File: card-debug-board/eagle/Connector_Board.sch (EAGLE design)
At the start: 37 parts, among them J1 ORESAT-DEBUG-CONNECTOR-CARD, J3 USB_A_SMT_FEMALE, Q1 MOSFET-PCH-SOT23-6, U1 FT230XS-R

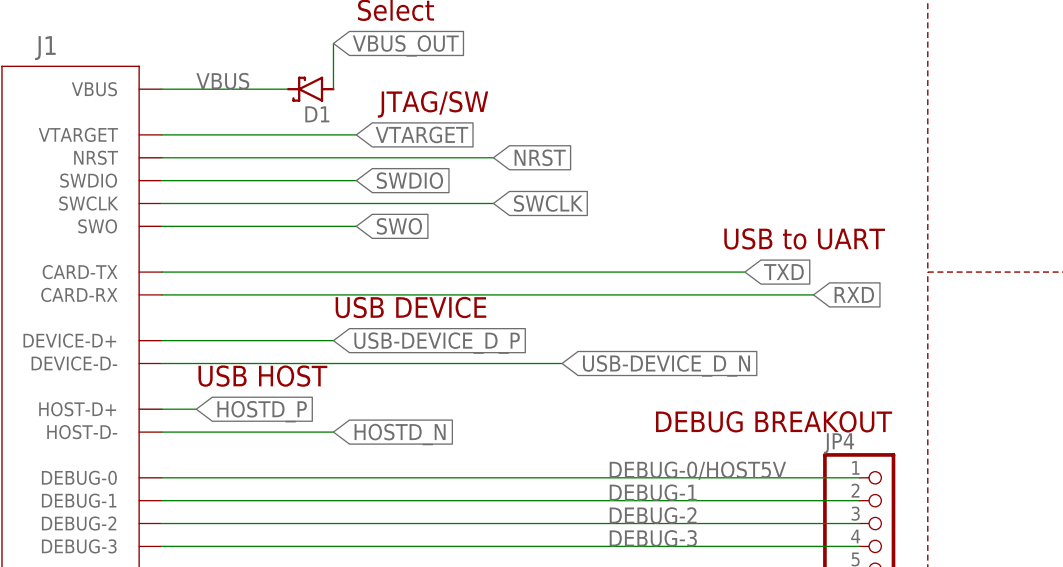
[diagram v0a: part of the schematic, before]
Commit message: Swapped TX RX traces
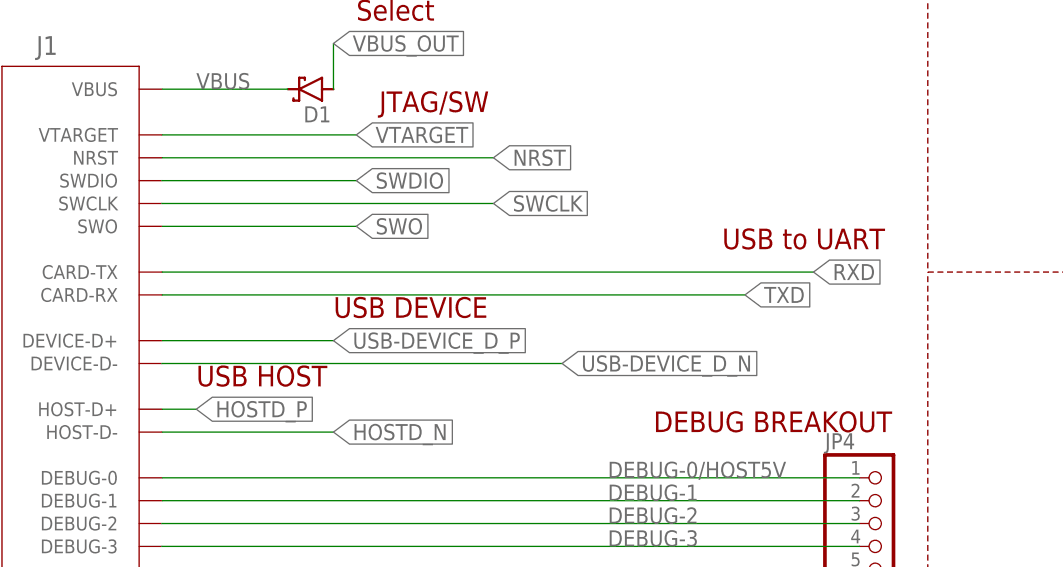
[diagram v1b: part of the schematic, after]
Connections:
- net RXD: now also J1.CARD-TX; no longer J1.CARD-RX
- net TXD: now also J1.CARD-RX; no longer J1.CARD-TX
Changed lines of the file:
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@@
 </segment>
 <segment>
-<label x="96.52" y="53.34" size="1.778" layer="95" xref="yes"/>
-<pinref part="J1" gate="G$1" pin="CARD-TX"/>
-<wire x1="31.75" y1="53.34" x2="96.52" y2="53.34" width="0.1524" layer="91"/>
+<label x="96.52" y="50.8" size="1.778" layer="95" xref="yes"/>
+<pinref part="J1" gate="G$1" pin="CARD-RX"/>
+<wire x1="31.75" y1="50.8" x2="96.52" y2="50.8" width="0.1524" layer="91"/>
 </segment>
 </net>
@@
 </segment>
 <segment>
-<label x="104.14" y="50.8" size="1.778" layer="95" xref="yes"/>
-<pinref part="J1" gate="G$1" pin="CARD-RX"/>
-<wire x1="31.75" y1="50.8" x2="104.14" y2="50.8" width="0.1524" layer="91"/>
+<label x="104.14" y="53.34" size="1.778" layer="95" xref="yes"/>
+<pinref part="J1" gate="G$1" pin="CARD-TX"/>
+<wire x1="31.75" y1="53.34" x2="104.14" y2="53.34" width="0.1524" layer="91"/>
 </segment>
 </net>

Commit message: updated the pin connectors
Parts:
- RX1, RX2, TX1, TX2: value (none) -> TEST-POINT-LARGE; device oresat-misc:TP1MM-TP -> oresat-misc:TEST-POINT-LARGE
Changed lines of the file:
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@@
 <layer number="136" name="silktop" color="7" fill="1" visible="yes" active="yes"/>
 <layer number="137" name="silkbottom" color="7" fill="1" visible="yes" active="yes"/>
+<layer number="138" name="mbTest" color="7" fill="1" visible="yes" active="yes"/>
+<layer number="139" name="mtKeepout" color="7" fill="1" visible="yes" active="yes"/>
 <layer number="140" name="Testjig_Mill" color="26" fill="1" visible="yes" active="yes"/>
+<layer number="141" name="mtRestrict" color="7" fill="1" visible="yes" active="yes"/>
+<layer number="142" name="mbRestrict" color="7" fill="1" visible="yes" active="yes"/>
+<layer number="143" name="mvRestrict" color="7" fill="1" visible="yes" active="yes"/>
 <layer number="144" name="Drill_legend" color="7" fill="1" visible="yes" active="yes"/>
 <layer number="145" name="DrillLegend_01-16" color="7" fill="1" visible="yes" active="yes"/>
 <layer number="146" name="DrillLegend_01-20" color="7" fill="1" visible="yes" active="yes"/>
+<layer number="147" name="mMeasures" color="7" fill="1" visible="yes" active="yes"/>
+<layer number="148" name="mDocument" color="7" fill="1" visible="yes" active="yes"/>
+<layer number="149" name="mReference" color="7" fill="1" visible="yes" active="yes"/>
 <layer number="150" name="Notes" color="7" fill="1" visible="yes" active="yes"/>
 <layer number="151" name="HeatSink" color="7" fill="1" visible="yes" active="yes"/>
@@
 <layer number="154" name="FabDoc2" color="7" fill="1" visible="yes" active="yes"/>
 <layer number="155" name="FabDoc3" color="7" fill="1" visible="yes" active="yes"/>
+<layer number="191" name="mNets" color="7" fill="1" visible="yes" active="yes"/>
+<layer number="192" name="mBusses" color="7" fill="1" visible="yes" active="yes"/>
+<layer number="193" name="mPins" color="7" fill="1" visible="yes" active="yes"/>
+<layer number="194" name="mSymbols" color="7" fill="1" visible="yes" active="yes"/>
+<layer number="195" name="mNames" color="7" fill="1" visible="yes" active="yes"/>
+<layer number="196" name="mValues" color="7" fill="1" visible="yes" active="yes"/>
 <layer number="199" name="Contour" color="7" fill="1" visible="yes" active="yes"/>
 <layer number="200" name="200bmp" color="7" fill="1" visible="yes" active="yes"/>
@@
 <part name="JP4" library="pinhead" library_urn="urn:adsk.eagle:library:325" deviceset="PINHD-1X5" device="" package3d_urn="urn:adsk.eagle:package:22469/2"/>
 <part name="R11" library="oresat-rcl" deviceset="R-US_" device="0603-C-NOSILK" value="10k"/>
-<part name="RX1" library="oresat-misc" deviceset="TP" device="1MM-TP" package3d_urn="urn:adsk.eagle:package:27946/1"/>
-<part name="RX2" library="oresat-misc" deviceset="TP" device="1MM-TP" package3d_urn="urn:adsk.eagle:package:27946/1"/>
-<part name="TX1" library="oresat-misc" deviceset="TP" device="1MM-TP" package3d_urn="urn:adsk.eagle:package:27946/1"/>
-<part name="TX2" library="oresat-misc" deviceset="TP" device="1MM-TP" package3d_urn="urn:adsk.eagle:package:27946/1"/>
+<part name="RX1" library="oresat-misc" deviceset="TEST-POINT-LARGE" device=""/>
+<part name="RX2" library="oresat-misc" deviceset="TEST-POINT-LARGE" device=""/>
+<part name="TX1" library="oresat-misc" deviceset="TEST-POINT-LARGE" device=""/>
+<part name="TX2" library="oresat-misc" deviceset="TEST-POINT-LARGE" device=""/>
 </parts>
 <sheets>

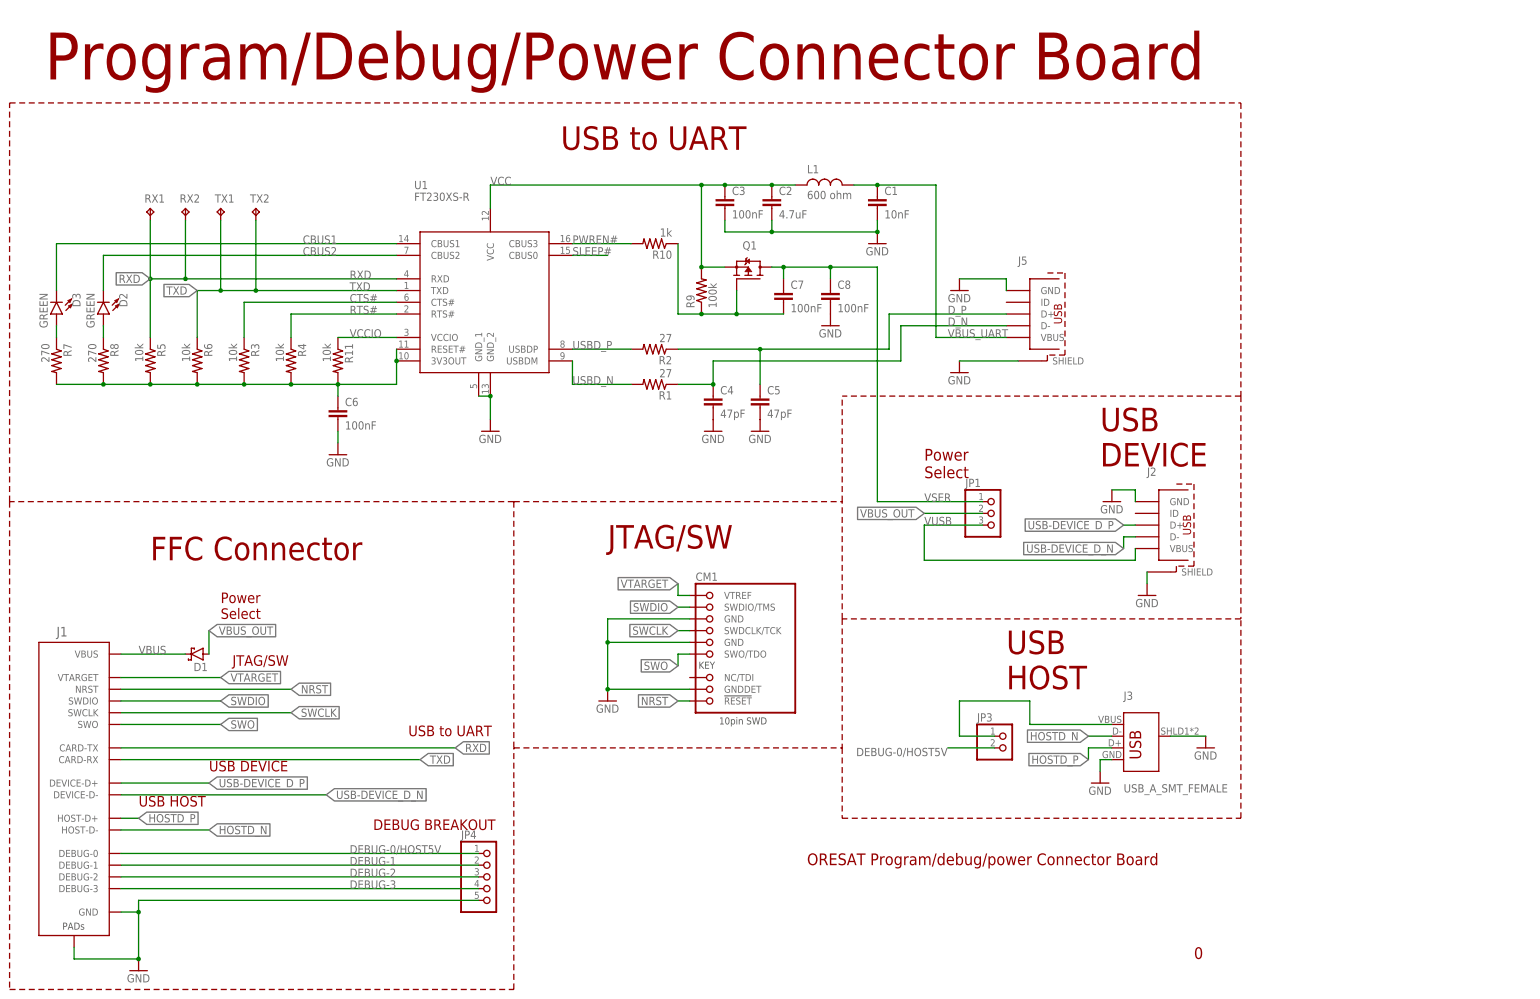
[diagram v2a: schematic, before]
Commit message: Version 1 of the OreSat debug board. Tinyified the board, added curved corners, centered FFC connector, added reset switch, made USB traces have a continuous ground plane, fixed FT203x VCCIO connection, made USB device shields not connected to ground as per spec, cleaned up silk screen.
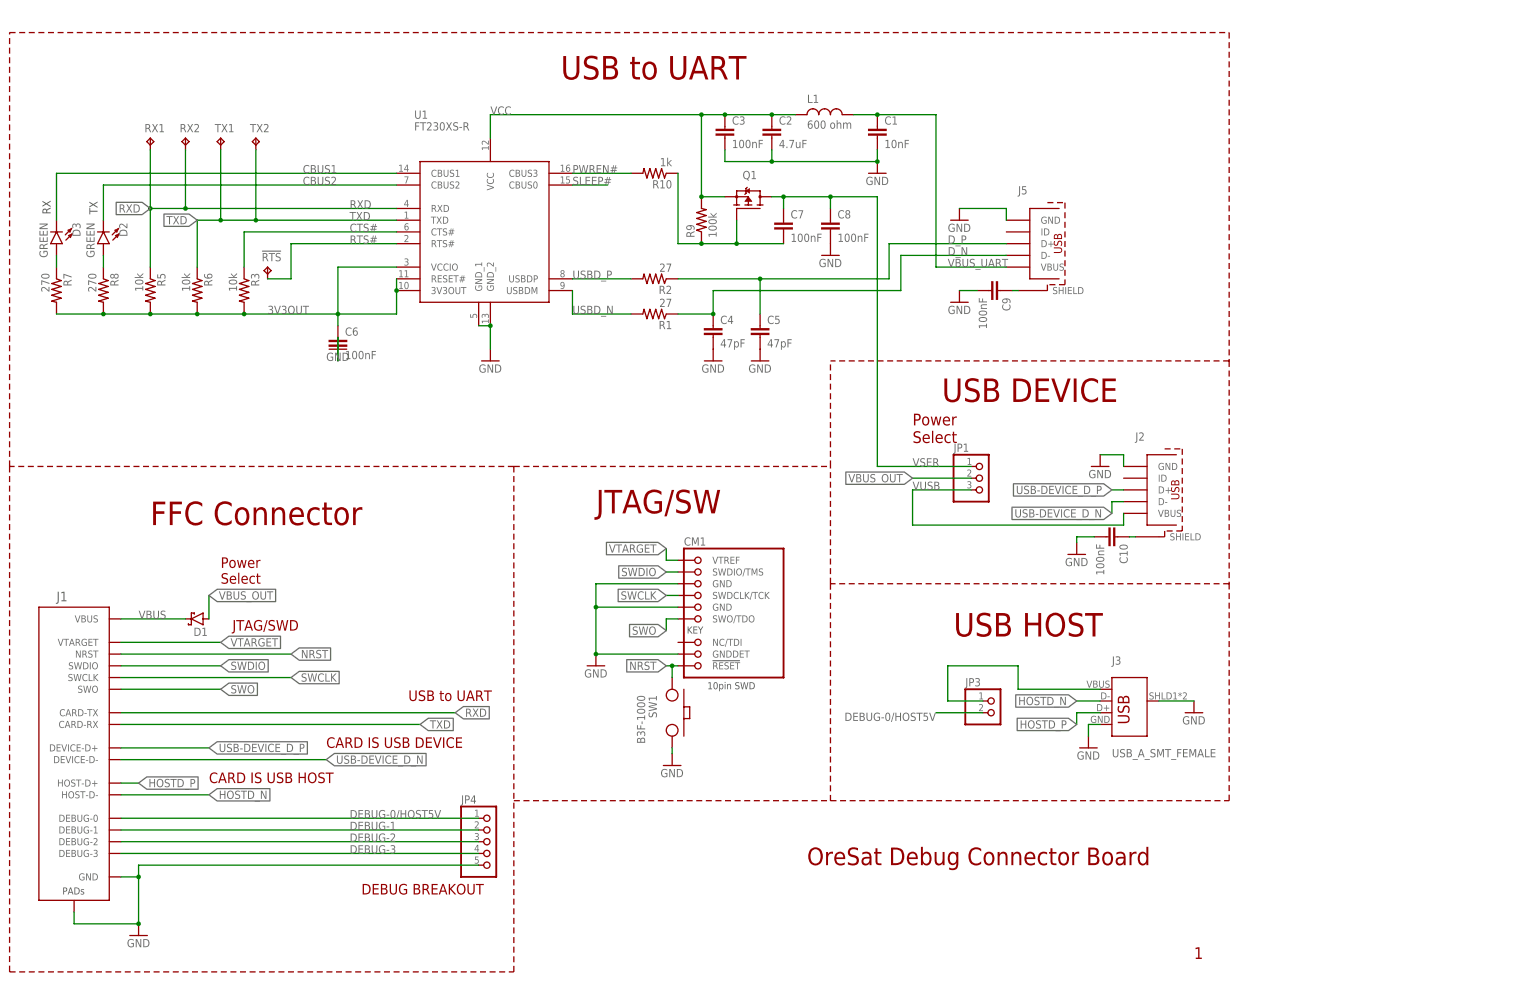
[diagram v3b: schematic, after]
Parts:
- removed R11, R4: 10k, oresat-rcl:R-US_0603-C-NOSILK
- added !RTS: TEST-POINT-LARGE, oresat-misc:TEST-POINT-LARGE
- added C10, C9: 100nF, oresat-rcl:C-EU0603-C-NOSILK
- added SW1: B3F-1000, apdm_ap_v2:SW-MOM-TACTILE-B3F-1000
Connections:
- removed net VCCIO: R11.1, U1.VCCIO
- removed net VCCIO_P: C6.1, R11.2, R3.2, R4.2, R5.2, R6.2, R7.2, R8.2, U1.3V3OUT, U1.RESET#
- new net 3V3OUT: C6.1, R3.2, R5.2, R6.2, R7.2, R8.2, U1.3V3OUT, U1.RESET#, U1.VCCIO
- new net N$1: C9.1, J5.SHIELD
- new net N$6: C10.1, J2.SHIELD
- net GND: now also C10.2, C9.2, SW1.2; no longer J2.SHIELD, J5.SHIELD
- net NRST: now also SW1.1
- net RTS#: now also !RTS.TP; no longer R4.1
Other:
- note added: "1"
- note added: "CARD IS USB DEVICE"
- note added: "CARD IS USB HOST"
- note added: "JTAG/SWD"
- note added: "OreSat Debug Connector Board"
- note added: "RX"
- note added: "TX"
- note removed: "0"
- note removed: "ORESAT Program/debug/power Connector Board"
- note removed: "Program/Debug/Power Connector Board"
- moved on the sheet: C1, C2, C3, C4, C5, C6, C7, C8, CM1, D1, D2, D3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

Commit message: Renamed VBUS to VBUSP added attributes to make BOM
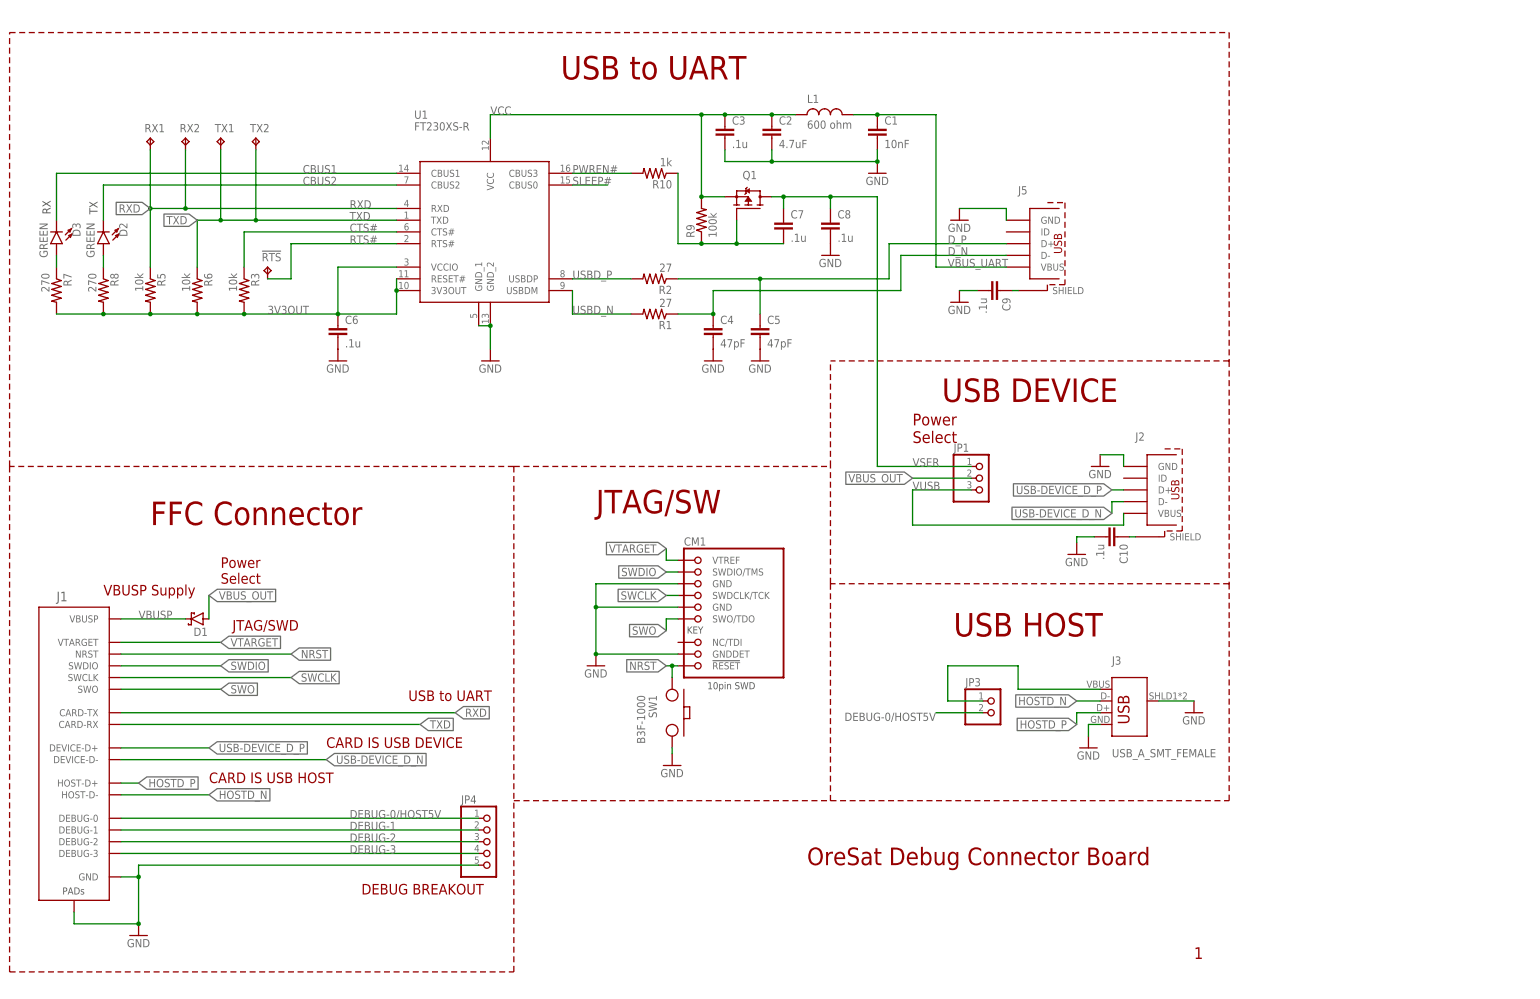
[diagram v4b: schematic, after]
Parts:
- C1: DESCRIPTION (none) -> 10000pF ±10% 50V Ceramic Capacitor X7R 0603 (1608 Metric); DIGI-KEY_PART_NUMBER (none) -> 732-13185-1-ND; MANUFACTURER (none) -> Wurth Elektronik; MANUFACTURER_PART_NUMBER (none) -> 885382206002; VDC (none) -> 50V
- C10, C3, C6, C7, C8, C9: value 100nF -> .1u; DESCRIPTION (none) -> 0.1µF ±10% 10V Ceramic Capacitor X5R 0603 (1608 Metric); DIGI-KEY_PART_NUMBER (none) -> 478-0603ZD104KAT2ACT-ND; MANUFACTURER (none) -> AVX; MANUFACTURER_PART_NUMBER (none) -> 0603ZD104KAT2A; VDC (none) -> 10V
- C2: DESCRIPTION (none) -> 4.7µF ±10% 10V Ceramic Capacitor X7S 0603 (1608 Metric); DIGI-KEY_PART_NUMBER (none) -> 445-14258-1-ND; MANUFACTURER (none) -> TDK; MANUFACTURER_PART_NUMBER (none) -> C1608X7S1A475K080AC; VDC (none) -> 10V
- C4, C5: DESCRIPTION (none) -> CAP CER 47PF 25V NP0 0603; DIGI-KEY_PART_NUMBER (none) -> 478-12679-1-ND; MANUFACTURER (none) -> AVX Corporation; MANUFACTURER_PART_NUMBER (none) -> 06033A470FAT2A; VDC (none) -> 25V
- CM1: DESCRIPTION (none) -> Connector Header Surface Mount 10 position 0.050" (1.27mm); DIGI-KEY_PART_NUMBER (none) -> SAM13160CT-ND; MANUFACTURER (none) -> Samtec Inc.; MANUFACTURER_PART_NUMBER (none) -> FTSH-105-01-F-DV-K-TR
- D1: DESCRIPTION (none) -> Diode Schottky 20V 500mA Surface Mount 0603/SOD-523F; DIGI-KEY_PART_NUMBER (none) -> 641-1332-1-ND; MANUFACTURER (none) -> Comchip Technology; MANUFACTURER_PART_NUMBER (none) -> CDBU0520
- D2, D3: DESCRIPTION (none) -> Green 573nm LED Indication - Discrete 2V 0603 (1608 Metric); DIGI-KEY_PART_NUMBER (none) -> 732-12017-1-ND; MANUFACTURER (none) -> Würth Elektronik; MANUFACTURER_PART_NUMBER (none) -> 150060VS55040
- J1: DESCRIPTION (none) -> 20 Position FPC Connector Contacts, Bottom 0.020" (0.50mm) 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; DIGI-KEY_PART_NUMBER (none) -> A100287CT-ND; MANUFACTURER (none) -> TE Connectivity AMP Connectors; MANUFACTURER_PART_NUMBER (none) -> 2-1734592-0
- J2, J5: DESCRIPTION (none) -> CONN RCPT USB2.0 MICRO B SMD R/A; DIGI-KEY_PART_NUMBER (none) -> 732-3155-1-ND; MANUFACTURER (none) -> Würth Elektronik; MANUFACTURER_PART_NUMBER (none) -> 629105136821
- J3: DESCRIPTION (none) -> SparkFun Accessories USB Female Type A SMD Connector; MANUFACTURER (none) -> SparkFun; MANUFACTURER_PART_NUMBER (none) -> PRT-09011; MOUSER_PART_NUMBER (none) -> 474-PRT-09011
- JP1: DESCRIPTION (none) -> CONN HEADER VERT 3POS 2.54MM; DIGI-KEY_PART_NUMBER (none) -> 732-5316-ND; MANUFACTURER (none) -> Würth Elektronik; MANUFACTURER_PART_NUMBER (none) -> 61300311121
- JP3: DESCRIPTION (none) -> Connector Header Through Hole 2 position 0.100" (2.54mm); DIGI-KEY_PART_NUMBER (none) -> 732-5315-ND; MANUFACTURER (none) -> Würth Elektronik; MANUFACTURER_PART_NUMBER (none) -> 61300211121
- JP4: DESCRIPTION (none) -> Connector Header Through Hole 5 position 0.100" (2.54mm); DIGI-KEY_PART_NUMBER (none) -> 732-5318-ND; MANUFACTURER (none) -> Würth Elektronik; MANUFACTURER_PART_NUMBER (none) -> 61300511121
- L1: DESCRIPTION (none) -> FERRITE BEAD 600 OHM 0805 1LN; DIGI-KEY_PART_NUMBER (none) -> 240-2390-1-ND; MANUFACTURER (none) -> Laird-Signal Integrity Products; MANUFACTURER_PART_NUMBER (none) -> MI0805K601R-10
- Q1: DESCRIPTION (none) -> P-Channel 30V 4.1A 350mW Surface Mount SOT-23-6L; DIGI-KEY_PART_NUMBER (none) -> SIL3407-TPMSCT-ND; MANUFACTURER (none) -> Micro Commercial Co; MANUFACTURER_PART_NUMBER (none) -> SIL3407-TP
- R1, R2: DESCRIPTION (none) -> RES SMD 27 OHM 1% 1/10W 0603; DIGI-KEY_PART_NUMBER (none) -> CR0603-FX-27R0ELFCT-ND; MANUFACTURER (none) -> Bourns Inc.; MANUFACTURER_PART_NUMBER (none) -> CR0603-FX-27R0ELF
- R10: DESCRIPTION (none) -> RES SMD 1K OHM 1% 1/10W 0603; DIGI-KEY_PART_NUMBER (none) -> 311-1.00KHRCT-ND; MANUFACTURER (none) -> Yageo; MANUFACTURER_PART_NUMBER (none) -> RC0603FR-071KL
- R3, R5, R6: DESCRIPTION (none) -> 10 kOhms ±1% 0.1W, 1/10W Chip Resistor 0603 (1608 Metric) M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; DIGI-KEY_PART_NUMBER (none) -> CR0603-FX-1002ELFCT-ND; MANUFACTURER (none) -> Bourns; MANUFACTURER_PART_NUMBER (none) -> CR0603-FX-1002ELF
- R7, R8: DESCRIPTION (none) -> RES SMD 270 OHM 1% 1/10W 0603; DIGI-KEY_PART_NUMBER (none) -> P270HCT-ND; MANUFACTURER (none) -> Panasonic Electronic Components; MANUFACTURER_PART_NUMBER (none) -> Panasonic Electronic Components
- R9: DESCRIPTION (none) -> 100 kOhms ±5% 0.1W, 1/10W Chip Resistor 0603 (1608 Metric) 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; DIGI-KEY_PART_NUMBER (none) -> RMCF0603JG100KTR-ND; MANUFACTURER (none) -> Stackpole Electronics Inc; MANUFACTURER_PART_NUMBER (none) -> RMCF0603JG100K
- SW1: DESCRIPTION (none) -> SWITCH TACTILE SPST-NO 0.05A 24V; DIGI-KEY_PART_NUMBER (none) -> SW400-ND; MANUFACTURER (none) -> Omron Electronics Inc-EMC Div; MANUFACTURER_PART_NUMBER (none) -> B3F-1000
- U1: DIGI-KEY_PART_NUMBER (none) -> 768-1135-1-ND
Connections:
- removed net VBUS: D1.C, J1.VBUS
- new net VBUSP: D1.C, J1.VBUSP
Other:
- note added: "VBUSP Supply"
- moved on the sheet: C6
